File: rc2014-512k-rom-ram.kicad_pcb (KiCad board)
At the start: 2 copper layers, 99.1 x 49.9 mm, 15 parts, among them J1 RC2014_Bus, U1 SST39SF040, U2 AS6C4008-55PCN, U3 74LS139, U4 74LS74, U5 74LS670, U6 74LS670, U7 74LS138

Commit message: OSHW logo
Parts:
- added REF**: OSHW-Logo2_9.8x8mm_SilkScreen, Symbol:OSHW-Logo2_9.8x8mm_SilkScreen, B.Cu at (156.2, 78.2)

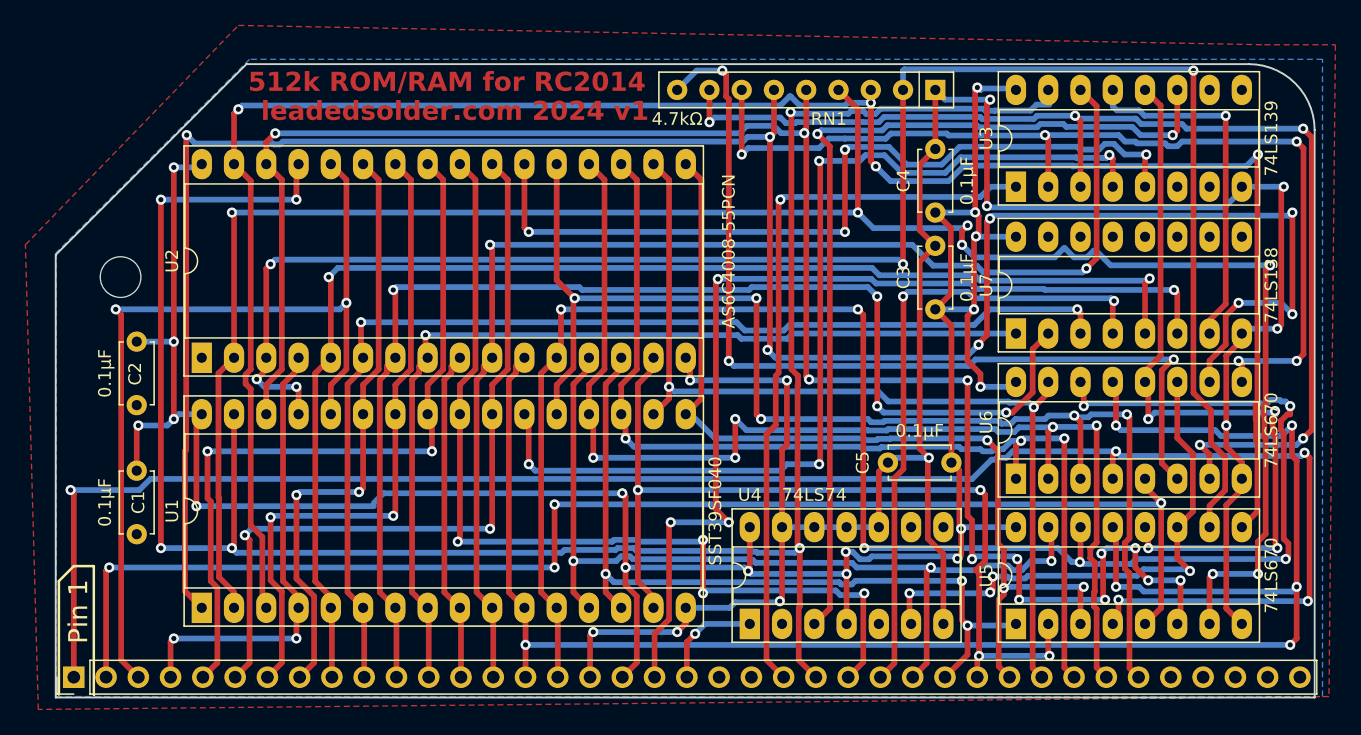
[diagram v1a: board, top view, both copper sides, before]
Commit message: Fix missing d0 line
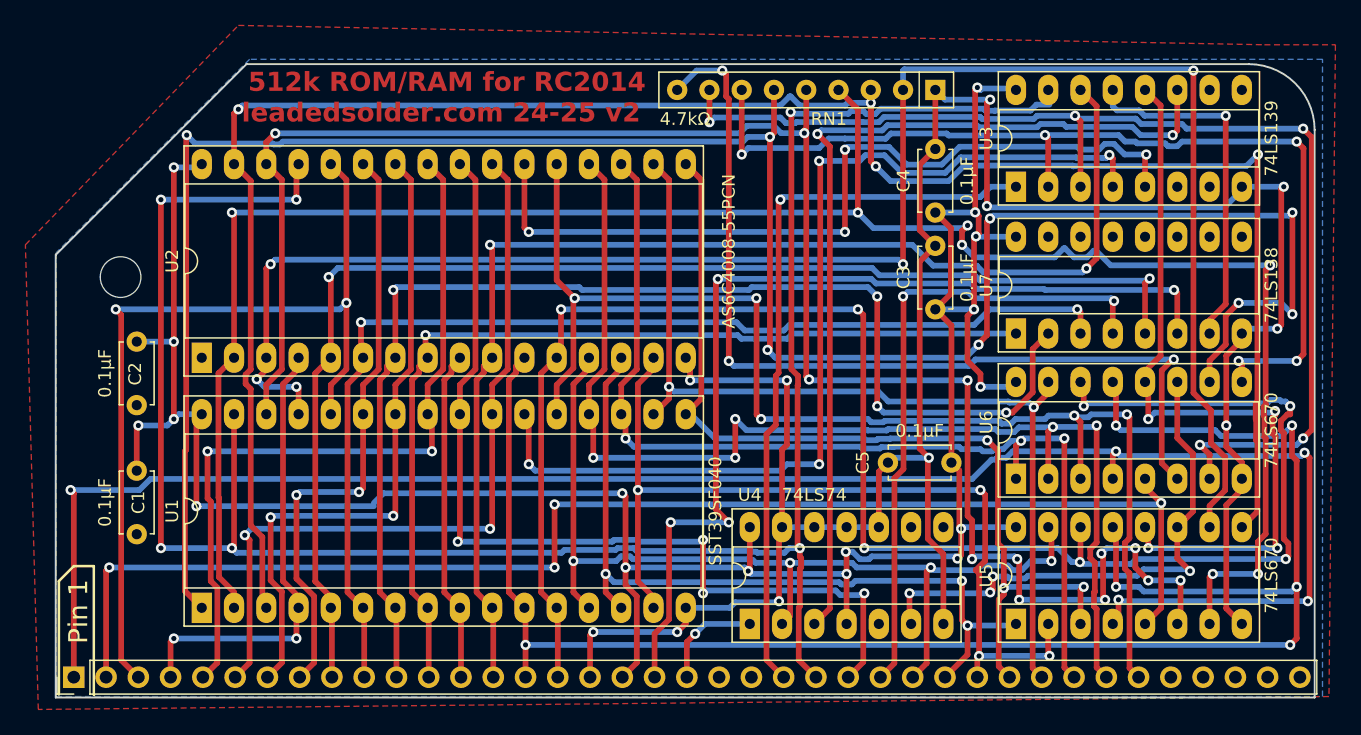
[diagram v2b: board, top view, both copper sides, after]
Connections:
- U4 pad 2: unconnected-(U4A-D-Pad2) -> /d0
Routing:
- net /d0: track 71.5 -> 76.6 mm, vias 3 -> 4
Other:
- board text added: "leadedsolder.com 24-25 v2"
- board text removed: "leadedsolder.com 2024 v1"

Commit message: A18 shouldn't be broken on 4008
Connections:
- U2 pad 1: unconnected-(U2-A18-Pad1) -> /ma18
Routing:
- net /ma18: track 176.3 -> 178.1 mm
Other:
- board text added: "~{CS}"
